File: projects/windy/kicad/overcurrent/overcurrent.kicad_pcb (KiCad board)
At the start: 2 copper layers, 50 x 100 mm, 71 parts, among them CON1 USB-MINI-B, P1 ISP, P2 SD_CARD, P3 ENCODER, Q1 Q_NMOS_GDS, Q2 Q_NMOS_GDS, Q3 Q_NMOS_GDS, SW1 RESET, SW2 HWB, U1 LM324, U2 ATMEGA32U4-A, U3 INA169, U4 74LS125, U5 DS1307, X1 32.768kHz

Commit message: big routing improvements
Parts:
- R8: value 20k -> 51k
- moved R18 48.8 mm to (68.5, 136.2), turned to 90 degrees
- moved R17 48.2 mm to (70.2, 136.2), turned to 270 degrees
- moved R20 33.9 mm to (62.2, 136.2), turned to 270 degrees
- moved R19 31.9 mm to (58.8, 136.2), turned to 270 degrees
- moved D5 31.1 mm to (60.5, 136.2), turned to 90 degrees
- moved C9 27.9 mm to (43.5, 119.5), turned to 180 degrees
- moved R7 23.3 mm to (50.8, 136.2), turned to 270 degrees
- moved C12 21.8 mm to (43.5, 92.8), turned to 270 degrees
- moved R6 21.1 mm to (47.2, 136.2), turned to 270 degrees
- moved D1 20.8 mm to (49.0, 136.2), turned to 90 degrees
- moved R8 20.5 mm to (66.2, 136.2), turned to 270 degrees
- moved R9 19.2 mm to (64.5, 136.2), turned to 90 degrees
- moved R11 18.4 mm to (56.5, 136.2), turned to 270 degrees
- moved R15 17.7 mm to (54.8, 114.2)
- moved R10 16.5 mm to (53.0, 136.2), turned to 270 degrees
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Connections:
- D7 pad 1: /REGULATED_LOAD -> Net-(D7-Pad1)
- R1 pad 1: Net-(C1-Pad2) -> Net-(R1-Pad1)
- R2 pad 1: Net-(C1-Pad2) -> Net-(R1-Pad1)
- U1 pad 3: Net-(C1-Pad2) -> Net-(D11-Pad1)
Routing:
- net VCC: track 153.5 -> 273.3 mm, vias 7 -> 10
- net /RESET: track 6.69 -> 60.1 mm, vias 0 -> 4
- net /CURR: track 0.65 -> 39.1 mm, vias 0 -> 2
- net Net-(D5-Pad1): track 5.49 -> 42.4 mm, vias 0 -> 2
- net /MOSI: track 36.3 -> 72.0 mm, vias 2 -> 6
- net Net-(D4-Pad1): track 5.25 -> 29.9 mm, vias 0 -> 2
- net /SWITCHED_SOURCE: track 25.0 -> 47.3 mm, vias 0 -> 1
- net /FILTERED_SOURCE: track 18.6 -> 31.1 mm, vias 0 -> 1
- net GND: track 94.7 -> 106.9 mm, vias 9 -> 19
- net Net-(D1-Pad1): track 5.25 -> 17.2 mm, vias 0 -> 2
- net /SWITCHED_LOAD: track 47.6 -> 36.1 mm, vias 1 -> 2
- net Net-(C1-Pad2): track 8.11 -> 3.66 mm
- net /SOURCE: track 53.1 -> 49.6 mm
- net Net-(D11-Pad1): track 0.00 -> 2.98 mm
- net /BATTERY: track 105.6 -> 108.3 mm
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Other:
- outline, holes or cut-outs redrawn
- board text added: "CHG"
- board text added: "DMP"
- board text added: "LD"

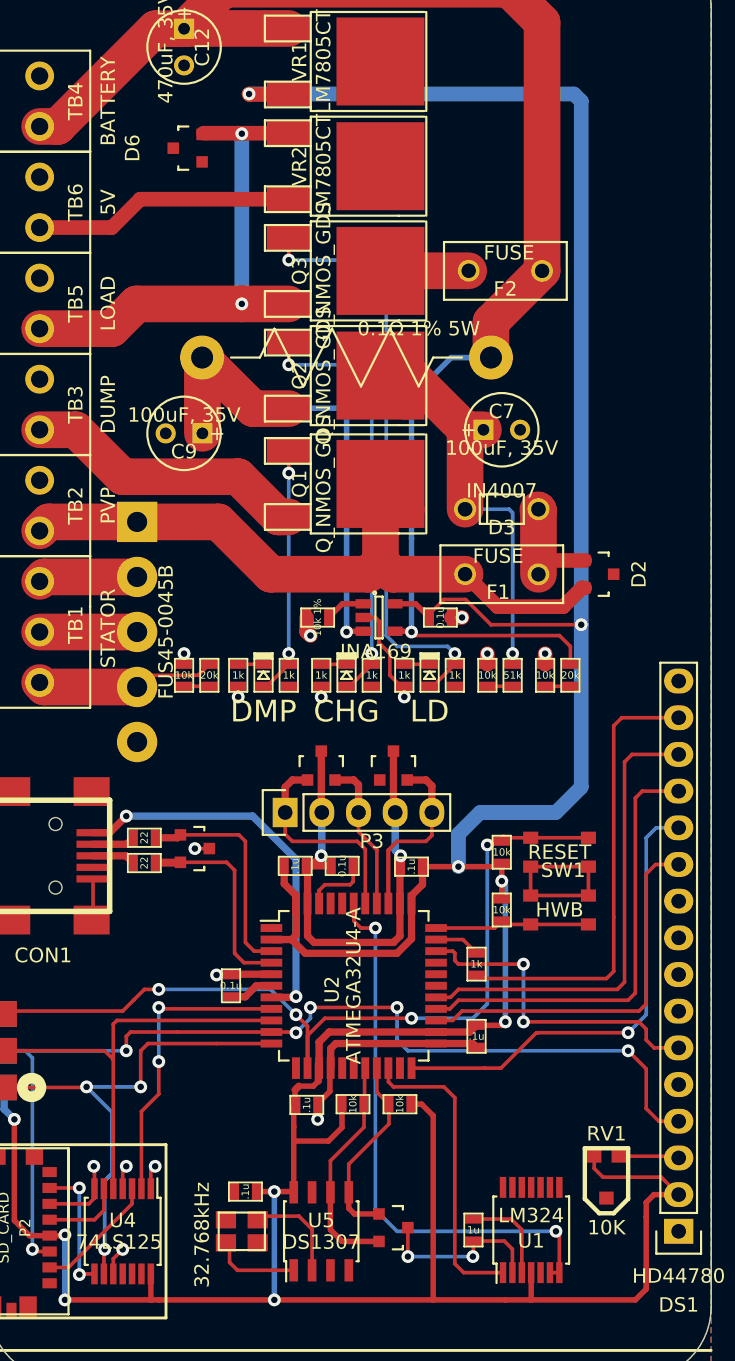
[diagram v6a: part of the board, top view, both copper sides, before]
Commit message: fully routed
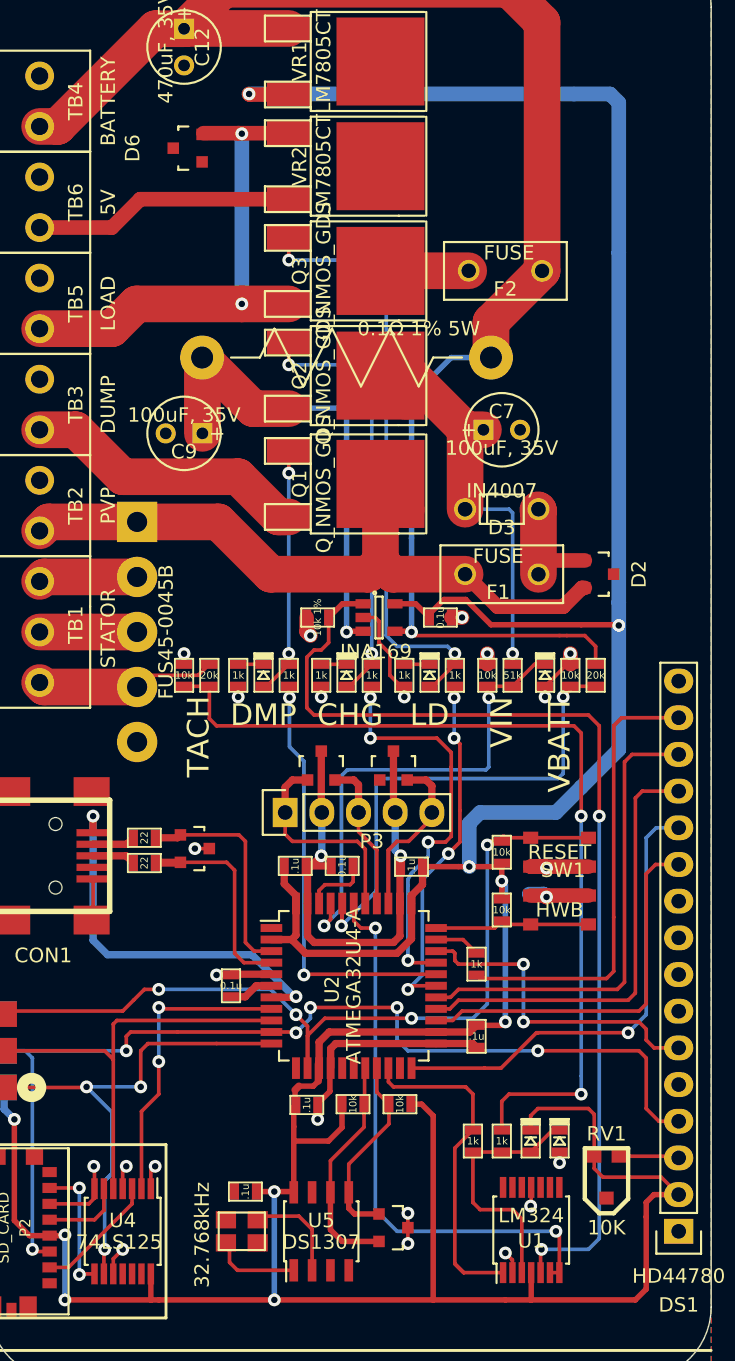
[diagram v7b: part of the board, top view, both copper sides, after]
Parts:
- removed C1: 1u, custom:SM0603_VALUE
- added D11: DSCHSMALL, custom:SM0603_DIODE, F.Cu at (67.5, 168.5)
- added D12: DSCHSMALL, custom:SM0603_DIODE, F.Cu at (69.5, 168.5)
- added D13: ZENERsmall, custom:SM0603_DIODE, F.Cu at (68.5, 136.2)
- added R21: 1k, custom:SM0603_VALUE, F.Cu at (65.5, 168.5)
- added R23: 1k, custom:SM0603_VALUE, F.Cu at (63.5, 168.5)
- moved R17 1.75 mm to (72.0, 136.2)
- moved R18 1.75 mm to (70.2, 136.2)
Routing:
- net Net-(R16-Pad1): track 2.78 -> 72.2 mm, vias 0 -> 2
- net Net-(R1-Pad1): track 1.75 -> 62.8 mm, vias 0 -> 2
- net /VBATT: track 1.75 -> 35.1 mm, vias 0 -> 2
- net /VIN: track 1.75 -> 33.3 mm, vias 0 -> 2
- net /DUMP_SW: track 0.00 -> 29.6 mm, vias 0 -> 2
- net /CHARGE_SW: track 0.00 -> 28.0 mm, vias 0 -> 4
- net /LOAD_SW: track 0.00 -> 24.7 mm, vias 0 -> 4
- net Net-(D11-Pad1): track 2.98 -> 17.7 mm
- net VCC: track 273.3 -> 287.9 mm
- net GND: track 106.9 -> 102.3 mm, vias 19 -> 25
- net Net-(C1-Pad2): track 3.66 -> 0.00 mm
- net /TACH: track 21.1 -> 23.9 mm
- net /BATTERY: track 108.3 -> 110.1 mm
- net /ENC_SW: track 16.1 -> 15.4 mm
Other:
- board text added: "TACH"
- board text added: "VBATT"
- board text added: "VIN"

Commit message: changing rtc component
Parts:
- U5: value DS1307 -> MCP7941X; footprint Housings_SOIC:SOIC-8_3.9x4.9mm_Pitch1.27mm -> Housings_SSOP:TSSOP-8_4.4x3mm_Pitch0.65mm
- moved U5 0.21 mm to (52.8, 174.8)
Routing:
- net /SDA: track 14.4 -> 16.0 mm
- net GND: track 102.3 -> 103.3 mm, vias 25 -> 26
- net Net-(U5-Pad1): track 6.27 -> 7.30 mm
- net /SCL: track 16.2 -> 17.1 mm
- net VCC: track 287.9 -> 288.7 mm
- net Net-(U5-Pad2): track 6.73 -> 7.48 mm
